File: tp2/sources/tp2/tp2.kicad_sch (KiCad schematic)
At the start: 21 parts, among them Q1 NPN, U2 ${SIM.PARAMS}, U3 ${SIM.PARAMS}, U4 ${SIM.PARAMS}, U5 ${SIM.PARAMS}, U6 ${SIM.PARAMS}

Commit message: tp2: agrega pcb
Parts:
- removed I1: ISIN, symbol Simulation_SPICE:ISIN
- removed U2, U3, U4, U5, U6: ${SIM.PARAMS}, symbol Simulation_SPICE:OPAMP
- added H1, H2, H3, H4, H5, H6: MountingHole_Pad, TestPoint:TestPoint_THTPad_2.0x2.0mm_Drill1.0mm, symbol Mechanical:MountingHole_Pad
- added R12: 680, Resistor_THT:R_Axial_DIN0207_L6.3mm_D2.5mm_P7.62mm_Horizontal, symbol Device:R
- added R13: Potentiometer, Potentiometer_THT:Potentiometer_Bourns_3266Y_Vertical, symbol Simulation_SPICE:Potentiometer
- added U1, U7: LM324, Package_DIP:DIP-14_W7.62mm_Socket, symbol Amplifier_Operational:LM324
- C1: footprint (none) -> Capacitor_THT:C_Rect_L7.2mm_W2.5mm_P5.00mm
- C2: value 270n -> 330n; footprint (none) -> Capacitor_THT:C_Rect_L7.2mm_W2.5mm_P5.00mm
- Q1: footprint (none) -> Package_TO_SOT_THT:TO-92
- R1, R10, R11, R2, R3, R4, R5, R6, R9: footprint (none) -> Resistor_THT:R_Axial_DIN0207_L6.3mm_D2.5mm_P7.62mm_Horizontal
- R7, R8: value 47k -> 33k; footprint (none) -> Resistor_THT:R_Axial_DIN0207_L6.3mm_D2.5mm_P7.62mm_Horizontal
- V1: now not fitted; now left out of the parts list
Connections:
- net 0: now also H3.1, U1.11 (V-), U7.11 (V-)
- net V+: now also H2.1, R12.1, U1.4 (V+), U7.4 (V+)
- net Vout_{1}: now also H4.1, U1.7
- net Vout_{filter}: now also H5.1, U1.8, U1.9 (-), U7.3 (+)
- net at R1.1, R2.1: now also H1.1, U1.3 (+)
- net V_{in}: now reaches R1.2
- net V_{in}: now also R13.2, R13.3, U1.12 (+)
- net at C2.2, R8.2: now also U1.10 (+)
- net at R3.2, R6.1: now also U1.6 (-)
- net at R4.2, R5.2: now also U1.5 (+)
- net at R3.1: now also U1.1, U1.2 (-)
- net at Q1.3 (E), R11.1: now also U7.2 (-)
- net at R4.1: now also U1.13 (-), U1.14
- net V_{C}: now reaches Q1.1 (C), R10.2
- net V_{C}: now also H6.1
- net at R9.2: now also U7.1
- new net: R12.2, R13.1

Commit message: tp2: agrega capacitores desacople y entrada alimentacion (xd)
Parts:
- added C3, C4: 100n, Capacitor_THT:C_Disc_D6.0mm_W2.5mm_P5.00mm, symbol Device:C
- added H7: MountingHole_Pad, TestPoint:TestPoint_THTPad_2.0x2.0mm_Drill1.0mm, symbol Mechanical:MountingHole_Pad
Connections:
- net 0: now also C3.2, C4.2
- net V+: now also C3.1, C4.1, H7.1; no longer H2.1, R12.1
- new net Vin: H2.1, R12.1
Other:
- moved on the sheet: H3, H4, H5, H6

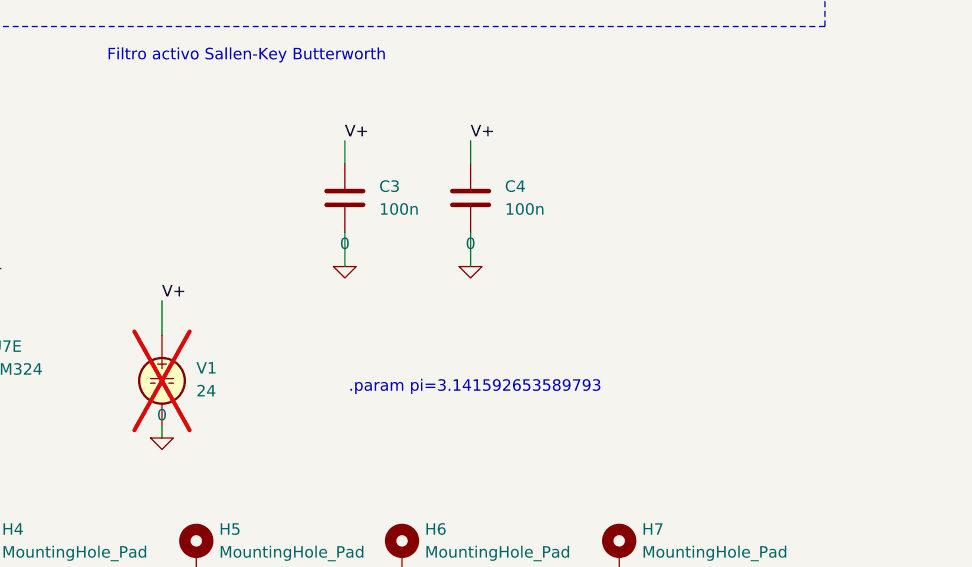
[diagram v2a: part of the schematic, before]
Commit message: tp2: agrega jumper entre Vcc y Vin
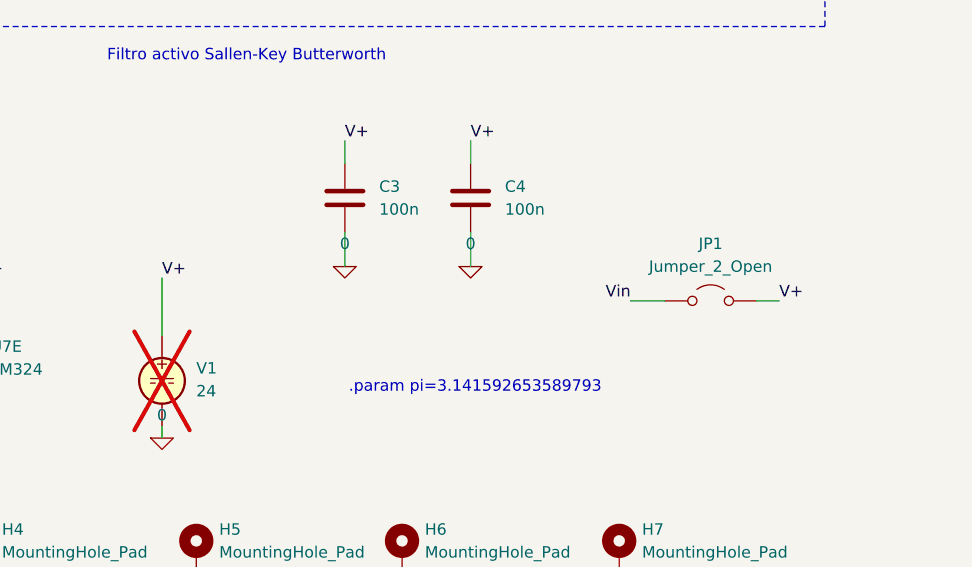
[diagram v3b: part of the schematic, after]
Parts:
- added JP1: Jumper_2_Open, Connector_PinHeader_2.54mm:PinHeader_1x02_P2.54mm_Vertical, symbol Jumper:Jumper_2_Open
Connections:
- net V+: now also JP1.2 (B)
- net Vin: now also JP1.1 (A)
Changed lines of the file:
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@@
 	(wire
 		(pts
-			(xy 209.55 127) (xy 209.55 130.81)
+			(xy 209.55 124.46) (xy 209.55 130.81)
 		)
 		(stroke
@@
 	(wire
 		(pts
+			(xy 275.59 127) (xy 278.13 127)
+		)
+		(stroke
+			(width 0)
+			(type default)
+		)
+	)
+	(wire
+		(pts
 			(xy 213.36 45.72) (xy 196.85 45.72)
 		)
@@
 		(pts
 			(xy 92.71 31.75) (xy 64.77 31.75)
+		)
+		(stroke
+			(width 0)
+			(type default)
+		)
+	)
+	(wire
+		(pts
+			(xy 261.62 127) (xy 265.43 127)
 		)
 		(stroke
@@
 		)
 	)
+	(label "V+"
+		(at 278.13 127 0)
+		(effects
+			(font
+				(size 1.27 1.27)
+			)
+			(justify left bottom)
+		)
+	)
 	(label "Vout_{filter}"
 		(at 213.36 161.29 0)
@@
 	)
 	(label "V+"
-		(at 209.55 127 0)
+		(at 209.55 124.46 0)
 		(effects
 			(font
@@
 			)
 			(justify left bottom)
+		)
+	)
+	(label "Vin"
+		(at 261.62 127 180)
+		(effects
+			(font
+				(size 1.27 1.27)
+			)
+			(justify right bottom)
 		)
 	)
@@
 				)
 			)
+		)
+	)
+	(symbol
+		(lib_id "Jumper:Jumper_2_Open")
+		(at 270.51 127 0)
+		(unit 1)
+		(body_style 1)
+		(exclude_from_sim no)
+		(in_bom yes)
+		(on_board yes)
+		(in_pos_files yes)
+		(dnp no)
+		(fields_autoplaced yes)
+		(property "Reference" "JP1"
+			(at 270.51 120.65 0)
+			(show_name no)
+			(do_not_autoplace no)
+			(effects
+				(font
+					(size 1.27 1.27)
+				)
+			)
+		)
+		(property "Value" "Jumper_2_Open"
+			(at 270.51 123.19 0)
+			(show_name no)
+			(do_not_autoplace no)
+			(effects
+				(font
+					(size 1.27 1.27)
+				)
+			)
+		)
+		(property "Footprint" "Connector_PinHeader_2.54mm:PinHeader_1x02_P2.54mm_Vertical"
+			(at 270.51 127 0)
+			(hide yes)
+			(show_name no)
+			(do_not_autoplace no)
+			(effects
+				(font
+					(size 1.27 1.27)
+				)
+			)
+		)
+		(property "Datasheet" ""
+			(at 270.51 127 0)
+			(hide yes)
+			(show_name no)
+			(do_not_autoplace no)
+			(effects
+				(font
+					(size 1.27 1.27)
+				)
+			)
+		)
+		(property "Description" "Jumper, 2-pole, open"
+			(at 270.51 127 0)
+			(hide yes)
+			(show_name no)
+			(do_not_autoplace no)
+			(effects
+				(font
+					(size 1.27 1.27)
+				)
+			)
+		)
+		(pin "1"
+		)
+		(pin "2"
+		)
+		(instances
+			(project "tp2"
+				(path "/c95402b1-5d65-4faa-a715-3078d768faff"
+					(reference "JP1")
+					(unit 1)
+				)
+			)

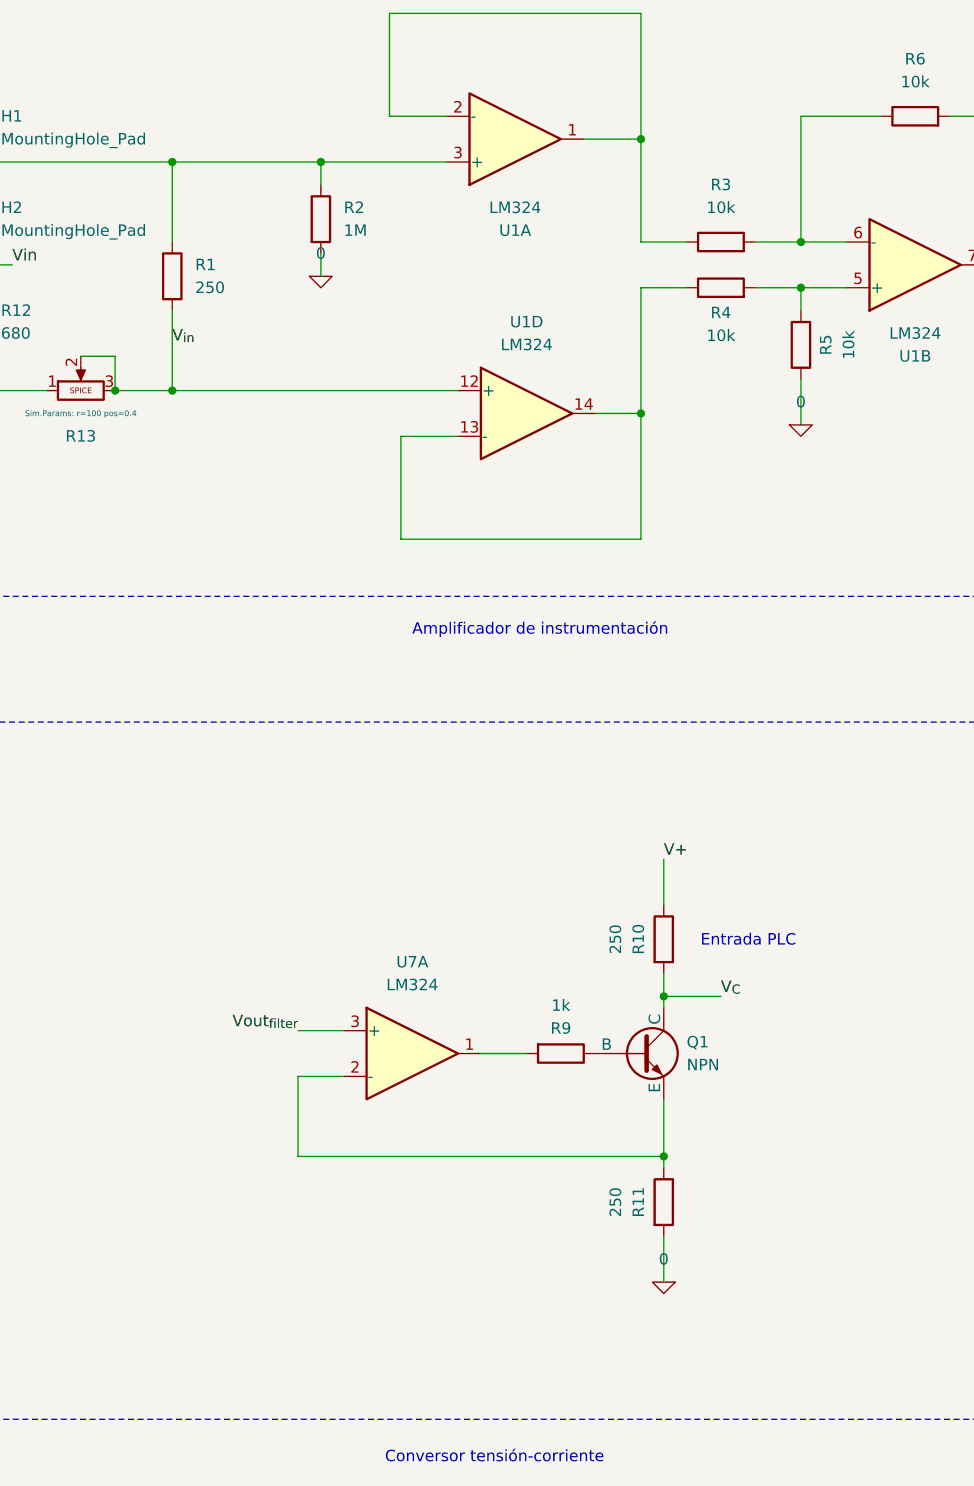
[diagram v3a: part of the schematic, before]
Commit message: tp2: reemplaza resistencias de 250ohm por (150+100)ohm
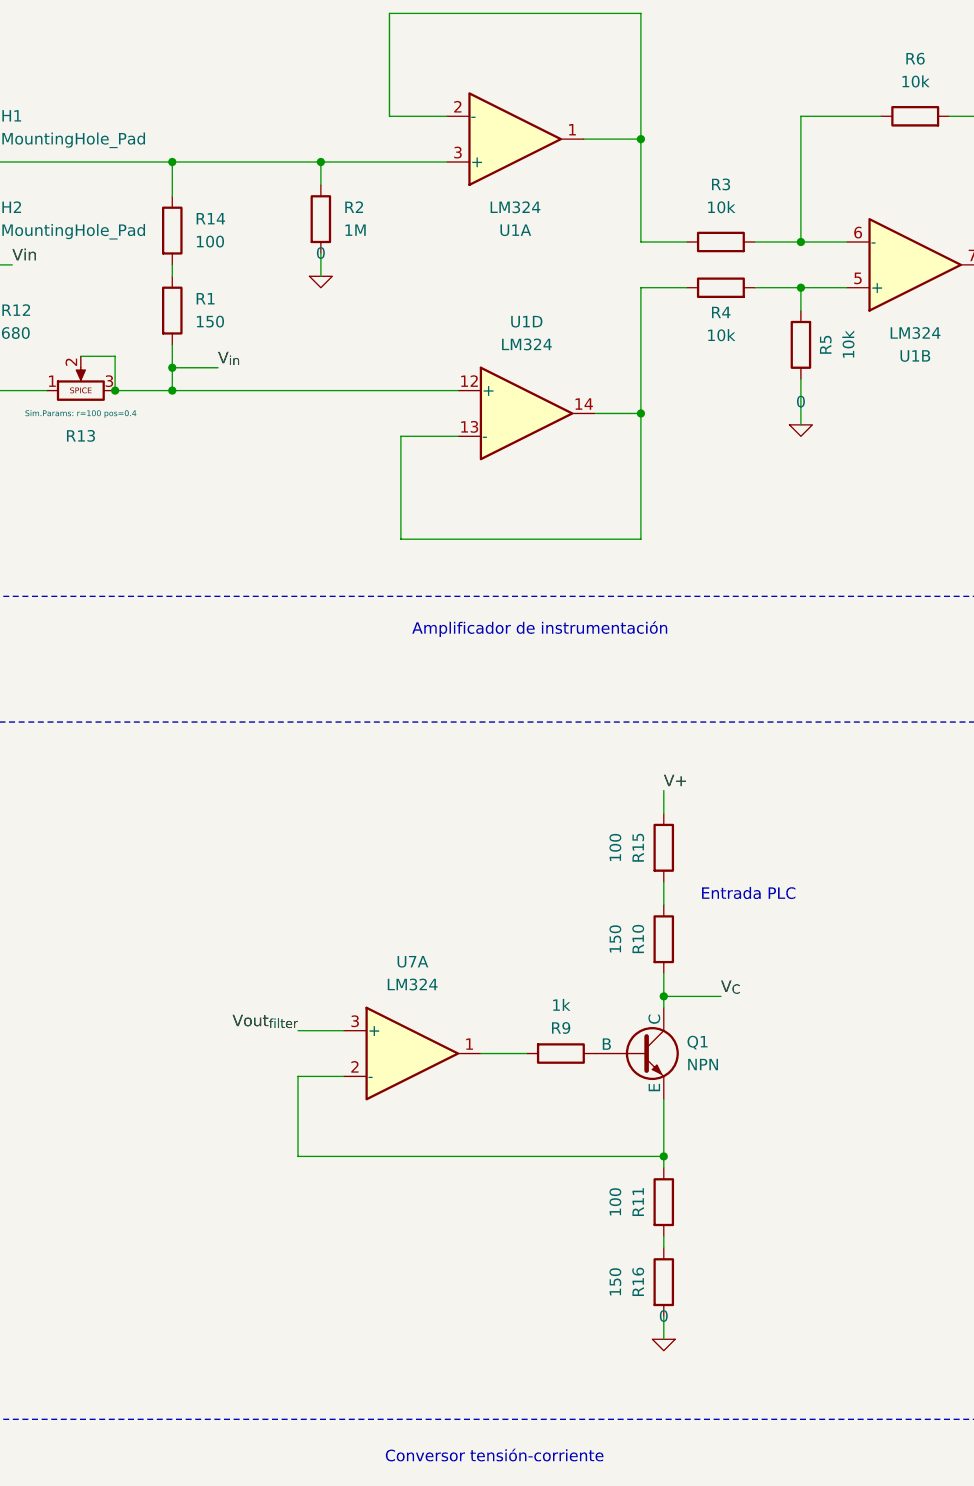
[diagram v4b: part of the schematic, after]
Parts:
- added R14, R15: 100, Resistor_THT:R_Axial_DIN0207_L6.3mm_D2.5mm_P7.62mm_Horizontal, symbol Device:R
- added R16: 150, Resistor_THT:R_Axial_DIN0207_L6.3mm_D2.5mm_P7.62mm_Horizontal, symbol Device:R
- R1, R10: value 250 -> 150
- R11: value 250 -> 100
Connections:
- net 0: now also R16.2; no longer R11.2
- net V+: now also R15.1; no longer R10.1
- net at H1.1, R2.1, U1.3 (+): now also R14.1; no longer R1.1
- new net: R1.1, R14.2
- new net: R11.2, R16.1
- new net: R10.1, R15.2
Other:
- moved on the sheet: R1

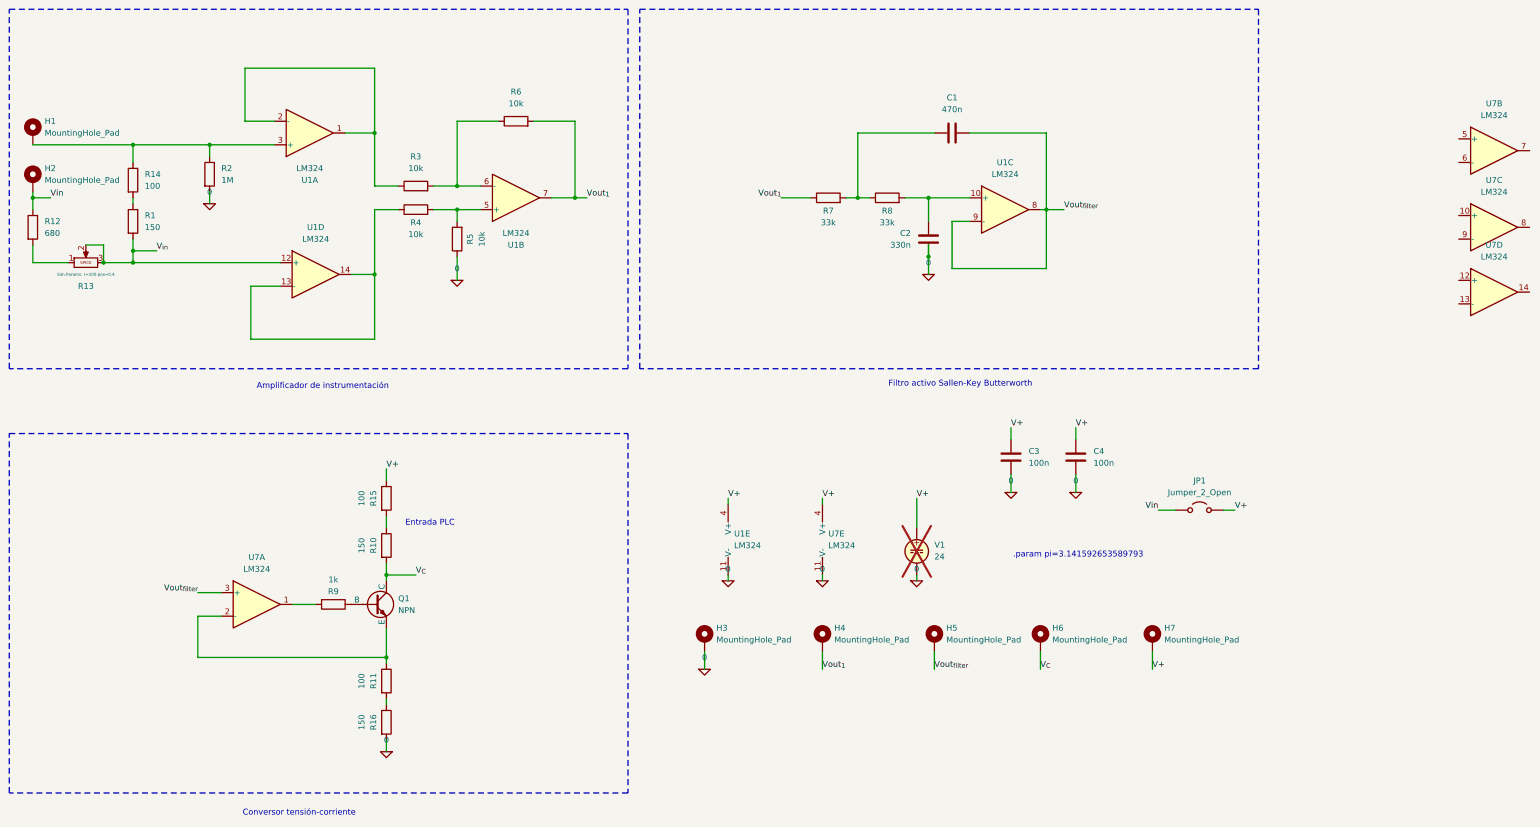
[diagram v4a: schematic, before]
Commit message: tp2: agrega jumper de gnd a la entrada Vin-
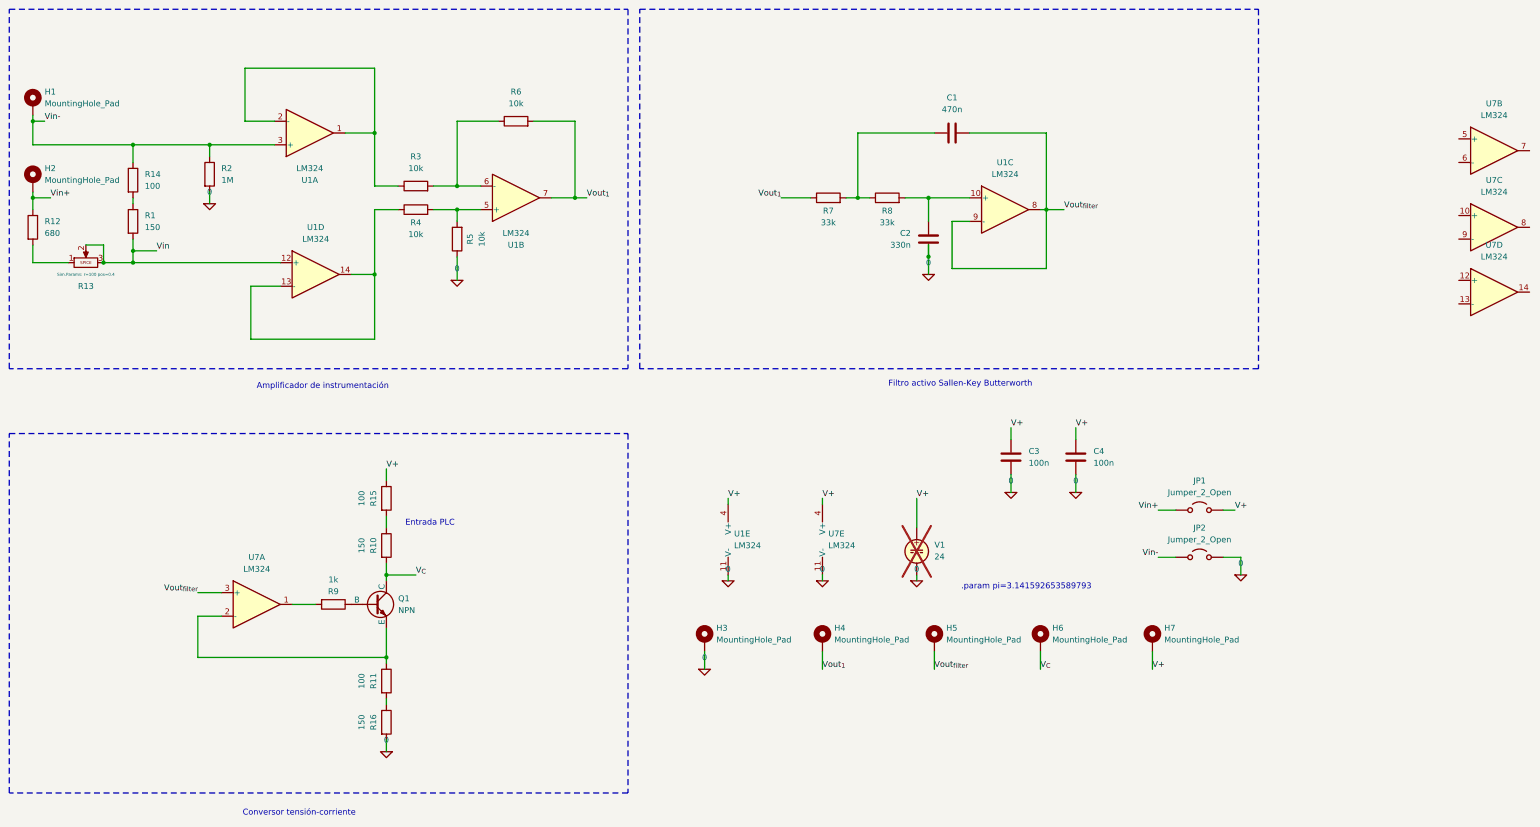
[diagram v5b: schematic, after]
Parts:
- added JP2: Jumper_2_Open, Connector_PinHeader_2.54mm:PinHeader_1x02_P2.54mm_Vertical, symbol Jumper:Jumper_2_Open
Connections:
- net V_{in} is gone; now on net Vin: R1.2, R13.2, R13.3, U1.12 (+)
- net 0: now also JP2.2 (B)
- net Vin: no longer H2.1, JP1.1 (A), R12.1
- net Vin-: now reaches H1.1, R14.1, R2.1, U1.3 (+)
- net Vin-: now also JP2.1 (A)
- new net Vin+: H2.1, JP1.1 (A), R12.1
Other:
- moved on the sheet: H1
